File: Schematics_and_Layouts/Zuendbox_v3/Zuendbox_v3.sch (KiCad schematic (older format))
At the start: 137 parts, among them J1 USB_B, J2 AVR-ISP-10, Q1 IRF3708, Q10 IRF3708, Q11 IRF3708, Q12 IRF3708, Q13 IRF3708, Q14 IRF3708, Q15 IRF3708, Q16 IRF3708, Q17 BC327, Q18 BC337, Q19 IRF4905, Q2 IRF3708, Q20 BC327, Q21 BC337, Q3 IRF3708, Q4 IRF3708, Q5 IRF3708, Q6 IRF3708, Q7 IRF3708, Q8 IRF3708, Q9 IRF3708, U1 DM13A, U10 DS18B20, U2 MCP6002-xP, U3 RFM69CW-RF_Module, U4 ATmega328P-PU, U5 74HC595, U6 XL6009_Module, U7 LM1084-3.3, U8 74HC595, U9 MCP2221_IP, Y1 Crystal

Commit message: KiCad version
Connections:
- wire segments 247 -> 253
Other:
- moved on the sheet: R11, R12, R13
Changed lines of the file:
@@
 EESchema Schematic File Version 4
+LIBS:Zuendbox_v3-cache
 EELAYER 26 0
 EELAYER END
@@
 Text Label 10300 2500 0    50   ~ 0
 MEAS_R_OUT
-Wire Wire Line
-	10250 1700 10700 1700
 Text Label 10350 1700 0    50   ~ 0
 SCK
-Wire Wire Line
-	10250 1600 10700 1600
-Wire Wire Line
-	10250 1500 10700 1500
 Text Label 10350 1600 0    50   ~ 0
 MISO
@@
 L Device:R R11
 U 1 1 5B6C48F7
-P 10850 1500
-F 0 "R11" V 10643 1500 50  0000 C CNN
-F 1 "1k" V 10734 1500 50  0000 C CNN
-F 2 "Resistor_THT:R_Axial_DIN0207_L6.3mm_D2.5mm_P10.16mm_Horizontal" V 10780 1500 50  0001 C CNN
-F 3 "~" H 10850 1500 50  0001 C CNN
-	1    10850 1500
+P 11950 900
+F 0 "R11" V 11743 900 50  0000 C CNN
+F 1 "1k" V 11834 900 50  0000 C CNN
+F 2 "Resistor_THT:R_Axial_DIN0207_L6.3mm_D2.5mm_P10.16mm_Horizontal" V 11880 900 50  0001 C CNN
+F 3 "~" H 11950 900 50  0001 C CNN
+	1    11950 900
 	0    1    1    0
 $EndComp
@@
 L Device:R R12
 U 1 1 5B6C4A44
-P 10850 1600
-F 0 "R12" V 10643 1600 50  0000 C CNN
-F 1 "1k" V 10734 1600 50  0000 C CNN
-F 2 "Resistor_THT:R_Axial_DIN0207_L6.3mm_D2.5mm_P10.16mm_Horizontal" V 10780 1600 50  0001 C CNN
-F 3 "~" H 10850 1600 50  0001 C CNN
-	1    10850 1600
+P 11950 1200
+F 0 "R12" V 11743 1200 50  0000 C CNN
+F 1 "1k" V 11834 1200 50  0000 C CNN
+F 2 "Resistor_THT:R_Axial_DIN0207_L6.3mm_D2.5mm_P10.16mm_Horizontal" V 11880 1200 50  0001 C CNN
+F 3 "~" H 11950 1200 50  0001 C CNN
+	1    11950 1200
 	0    1    1    0
 $EndComp
@@
 L Device:R R13
 U 1 1 5B6C4AAC
-P 10850 1700
-F 0 "R13" V 10643 1700 50  0000 C CNN
-F 1 "1k" V 10734 1700 50  0000 C CNN
-F 2 "Resistor_THT:R_Axial_DIN0207_L6.3mm_D2.5mm_P10.16mm_Horizontal" V 10780 1700 50  0001 C CNN
-F 3 "~" H 10850 1700 50  0001 C CNN
-	1    10850 1700
+P 12200 1450
+F 0 "R13" V 11993 1450 50  0000 C CNN
+F 1 "1k" V 12084 1450 50  0000 C CNN
+F 2 "Resistor_THT:R_Axial_DIN0207_L6.3mm_D2.5mm_P10.16mm_Horizontal" V 12130 1450 50  0001 C CNN
+F 3 "~" H 12200 1450 50  0001 C CNN
+	1    12200 1450
 	0    1    1    0
 $EndComp
 Wire Wire Line
-	11000 1500 11550 1500
+	12100 900  12750 900
 Wire Wire Line
-	11000 1600 11550 1600
+	12100 1200 12750 1200
 Wire Wire Line
-	11000 1700 11550 1700
-Text Label 11050 1500 0    50   ~ 0
+	12350 1450 12750 1450
+Text Label 12250 900  0    50   ~ 0
 MOSI_BUS
-Text Label 11050 1600 0    50   ~ 0
+Text Label 12250 1200 0    50   ~ 0
 MISO_BUS
-Text Label 11050 1700 0    50   ~ 0
+Text Label 12400 1450 0    50   ~ 0
 SCK_BUS
 $Comp
@@
 Text Notes 8000 10150 0    118  ~ 0
 USB-Interface
+Wire Wire Line
+	10250 1500 11550 1500
+Wire Wire Line
+	11550 1500 11550 900
+Wire Wire Line
+	11550 900  11800 900
+Wire Wire Line
+	11650 1600 11650 1200
+Wire Wire Line
+	11650 1200 11800 1200
+Wire Wire Line
+	10250 1600 11650 1600
+Wire Wire Line
+	11750 1700 11750 1450
+Wire Wire Line
+	11750 1450 12050 1450
+Wire Wire Line
+	10250 1700 11750 1700
 $EndSCHEMATC

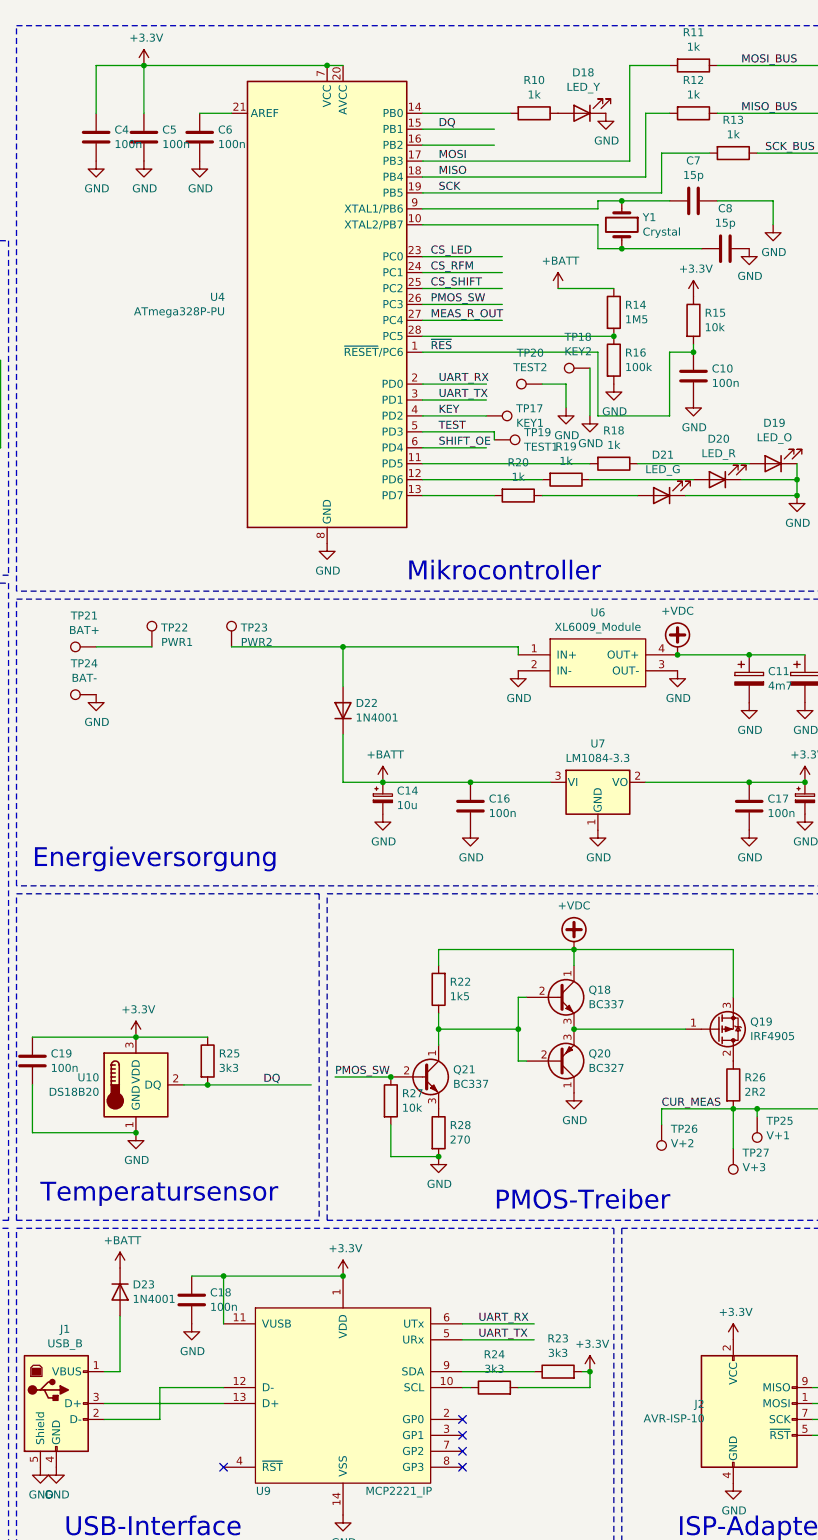
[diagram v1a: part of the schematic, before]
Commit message: Changed RF parameters (smaller deviation, smaller rx bandwidth)
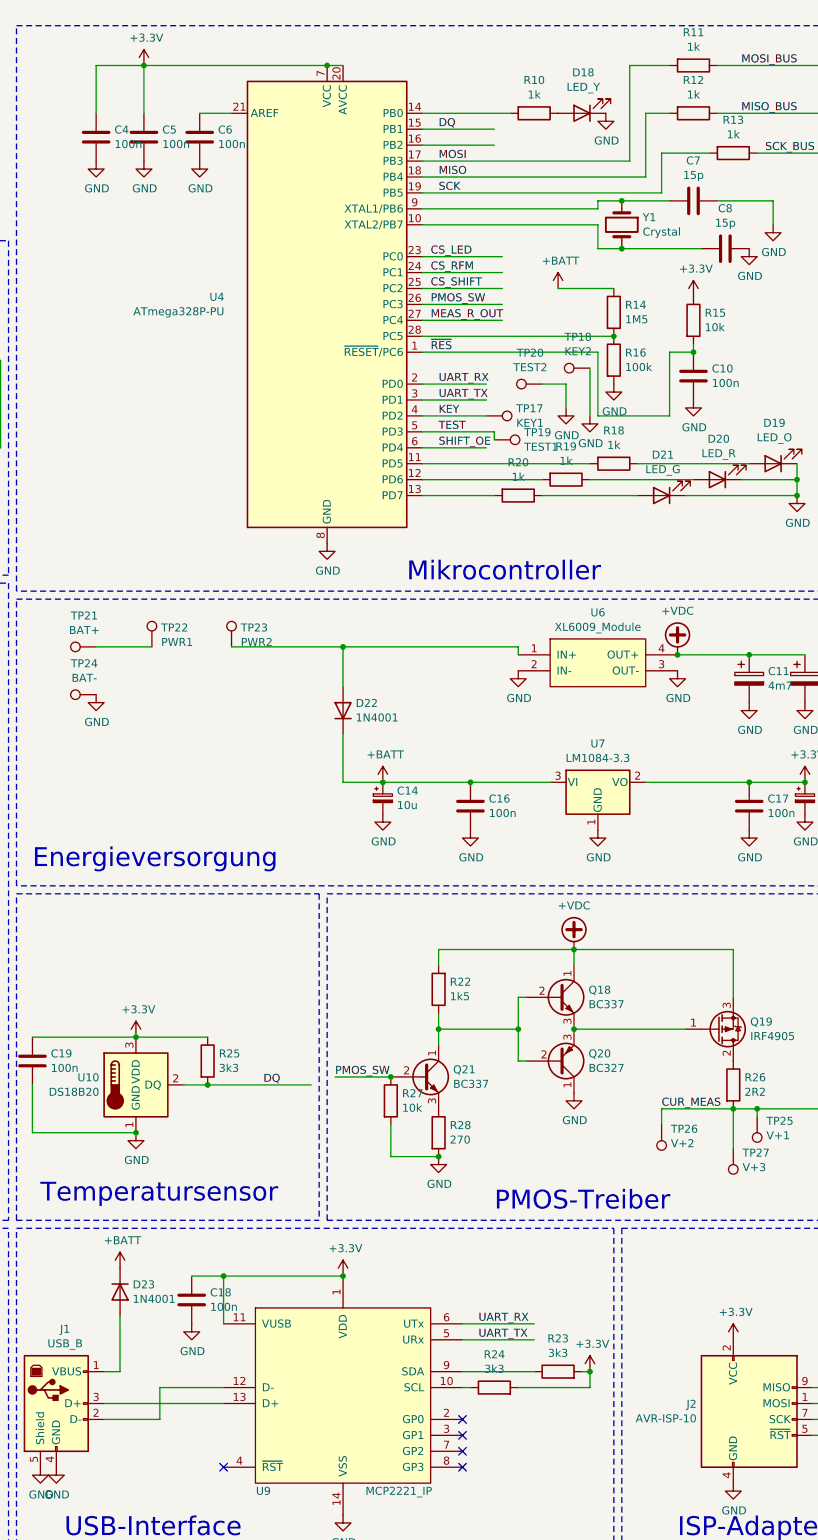
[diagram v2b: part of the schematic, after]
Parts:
- J2: footprint Connector_IDC:IDC-Header_2x05_P2.54mm_Vertical -> (none)
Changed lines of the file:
@@
-EESchema Schematic File Version 4
-LIBS:Zuendbox_v3-cache
-EELAYER 26 0
+EESchema Schematic File Version 5
+EELAYER 30 0
 EELAYER END
 $Descr User 13780 12205
@@
 Comment3 ""
 Comment4 ""
+Comment5 ""
+Comment6 ""
+Comment7 ""
+Comment8 ""
+Comment9 ""
 $EndDescr
 $Comp
@@
 $EndComp
 $Comp
-L MCU_Microchip_ATmega:ATmega328P-PU U4
-U 1 1 5B6A7BC1
-P 9650 2400
-F 0 "U4" H 9009 2446 50  0000 R CNN
-F 1 "ATmega328P-PU" H 9009 2355 50  0000 R CNN
-F 2 "Package_DIP:DIP-28_W7.62mm" H 9650 2400 50  0001 C CIN
-F 3 "http://ww1.microchip.com/downloads/en/DeviceDoc/ATmega328_P%20AVR%20MCU%20with%20picoPower%20Technology%20Data%20Sheet%2040001984A.pdf" H 9650 2400 50  0001 C CNN
-	1    9650 2400
-	1    0    0    -1
-$EndComp
-$Comp
 L Device:C C6
 U 1 1 5B6A8164
@@
 	8500 1200 8500 900
 Wire Wire Line
-	8500 900  9650 900
-Wire Wire Line
 	8200 1200 8200 900
 Wire Wire Line
@@
 	1    0    0    -1
 $EndComp
-Wire Wire Line
-	9650 900  9750 900
-Connection ~ 9650 900
 $Comp
 L power:GND #PWR040
@@
 $EndComp
 $Comp
-L Connector:AVR-ISP-10 J2
-U 1 1 5B781453
-P 12300 9400
-F 0 "J2" H 12020 9496 50  0000 R CNN
-F 1 "AVR-ISP-10" H 12020 9405 50  0000 R CNN
-F 2 "Connector_IDC:IDC-Header_2x05_P2.54mm_Vertical" V 12050 9450 50  0001 C CNN
-F 3 " ~" H 11025 8850 50  0001 C CNN
-	1    12300 9400
-	1    0    0    -1
-$EndComp
-$Comp
 L power:GND #PWR086
 U 1 1 5B781D39
@@
 Wire Wire Line
 	10250 1700 11750 1700
+Wire Wire Line
+	8500 900  9650 900
+$Comp
+L MCU_Microchip_ATmega:ATmega328P-PU U4
+U 1 1 5E9BA35A
+P 9650 2400
+F 0 "U4" H 9005 2446 50  0000 R CNN
+F 1 "ATmega328P-PU" H 9005 2355 50  0000 R CNN
+F 2 "Package_DIP:DIP-28_W7.62mm" H 9650 2400 50  0001 C CIN
+F 3 "http://ww1.microchip.com/downloads/en/DeviceDoc/ATmega328_P%20AVR%20MCU%20with%20picoPower%20Technology%20Data%20Sheet%2040001984A.pdf" H 9650 2400 50  0001 C CNN
+	1    9650 2400
+	1    0    0    -1
+$EndComp
+Wire Wire Line
+	9750 900  9650 900
+Connection ~ 9650 900
+$Comp
+L Connector:AVR-ISP-10 J2
+U 1 1 5E9D4123
+P 12300 9400
+F 0 "J2" H 11970 9496 50  0000 R CNN
+F 1 "AVR-ISP-10" H 11970 9405 50  0000 R CNN
+F 2 "" V 12050 9450 50  0001 C CNN
+F 3 " ~" H 11025 8850 50  0001 C CNN
+	1    12300 9400
+	1    0    0    -1
+$EndComp
 $EndSCHEMATC
